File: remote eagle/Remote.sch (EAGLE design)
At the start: 30 parts, among them J1 ISP Touch, Y1 16MHz, Y2 ANTENNA2SMD5

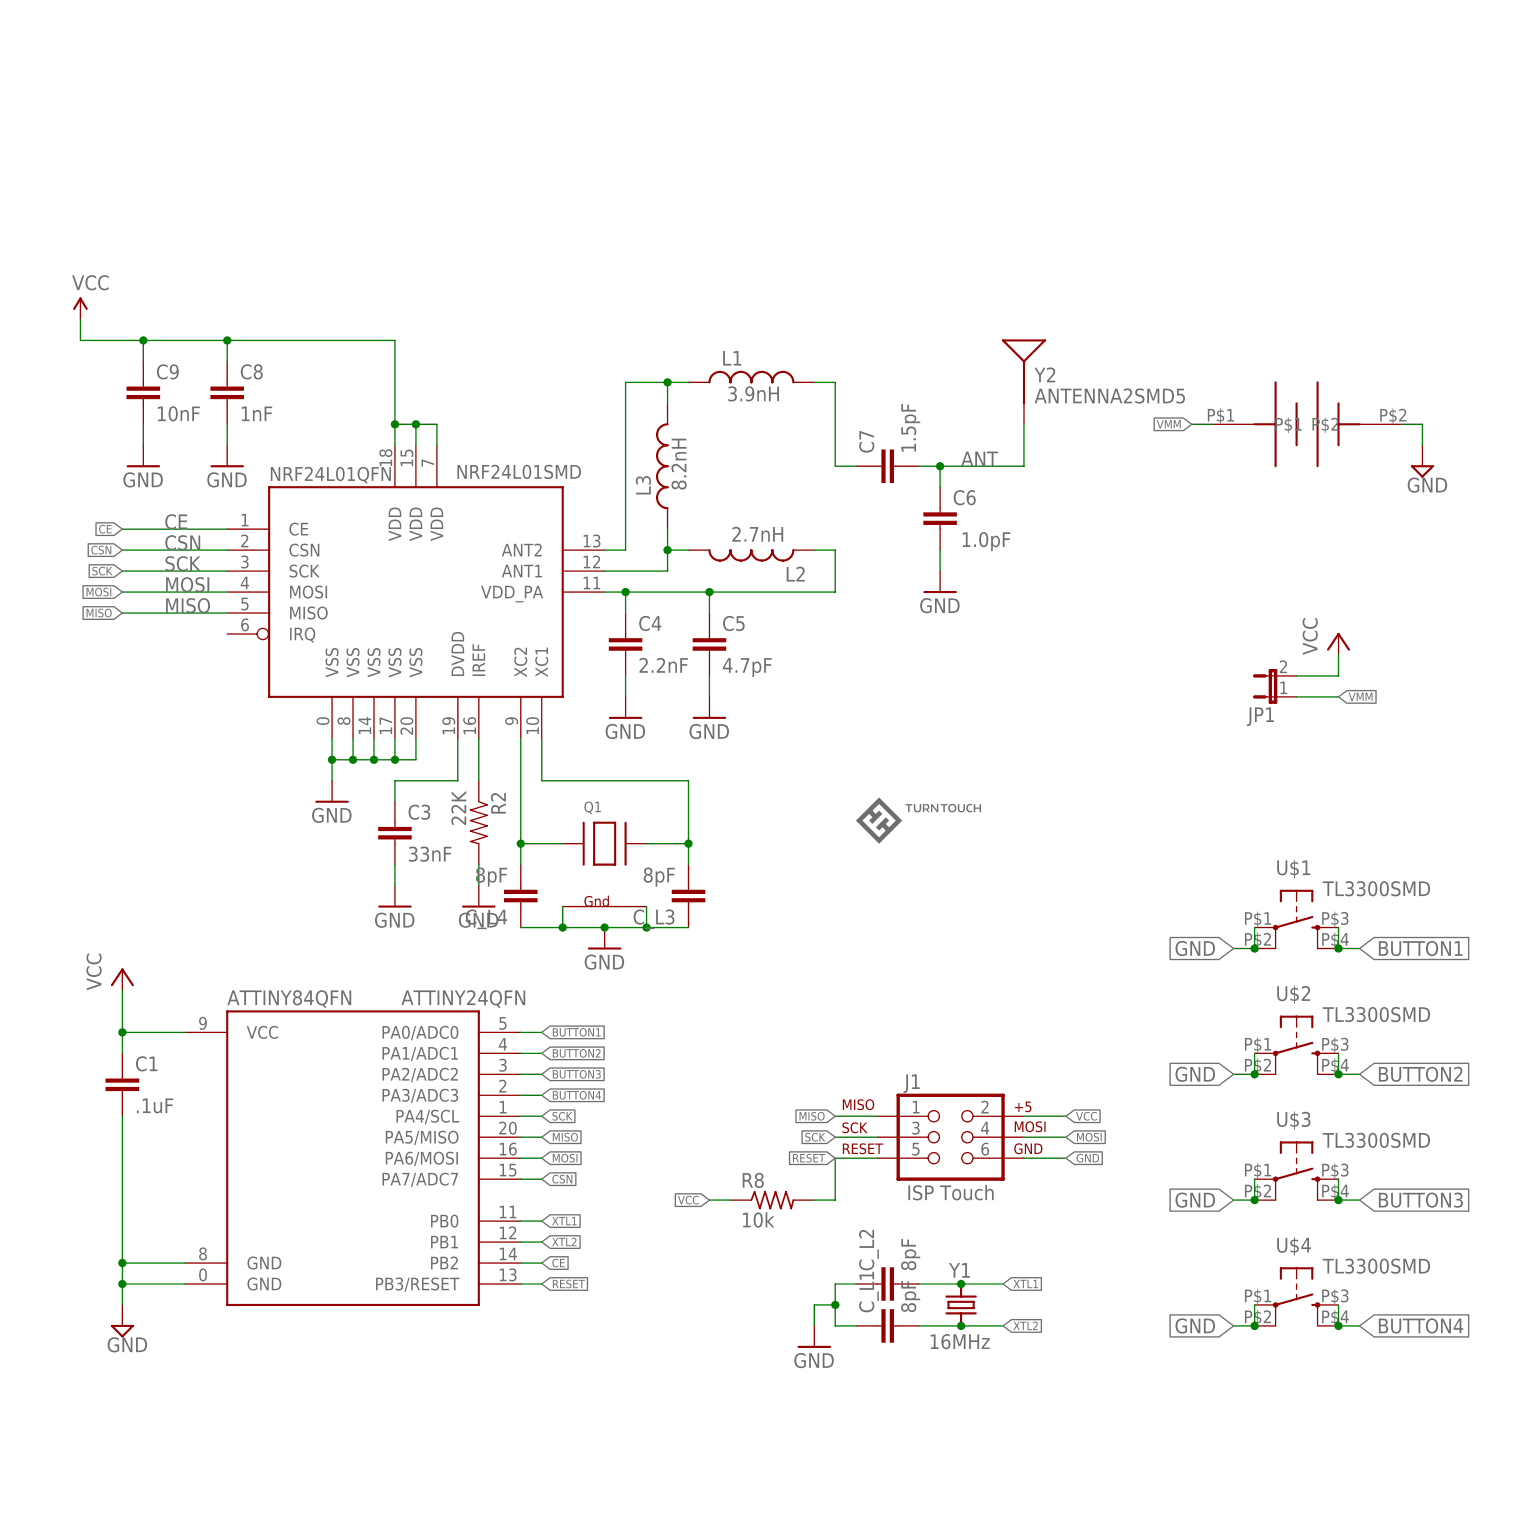
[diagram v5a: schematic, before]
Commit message: Revision 9 of the board. Could perhaps use some tweaking. Now uses atmega328p qfn chip.
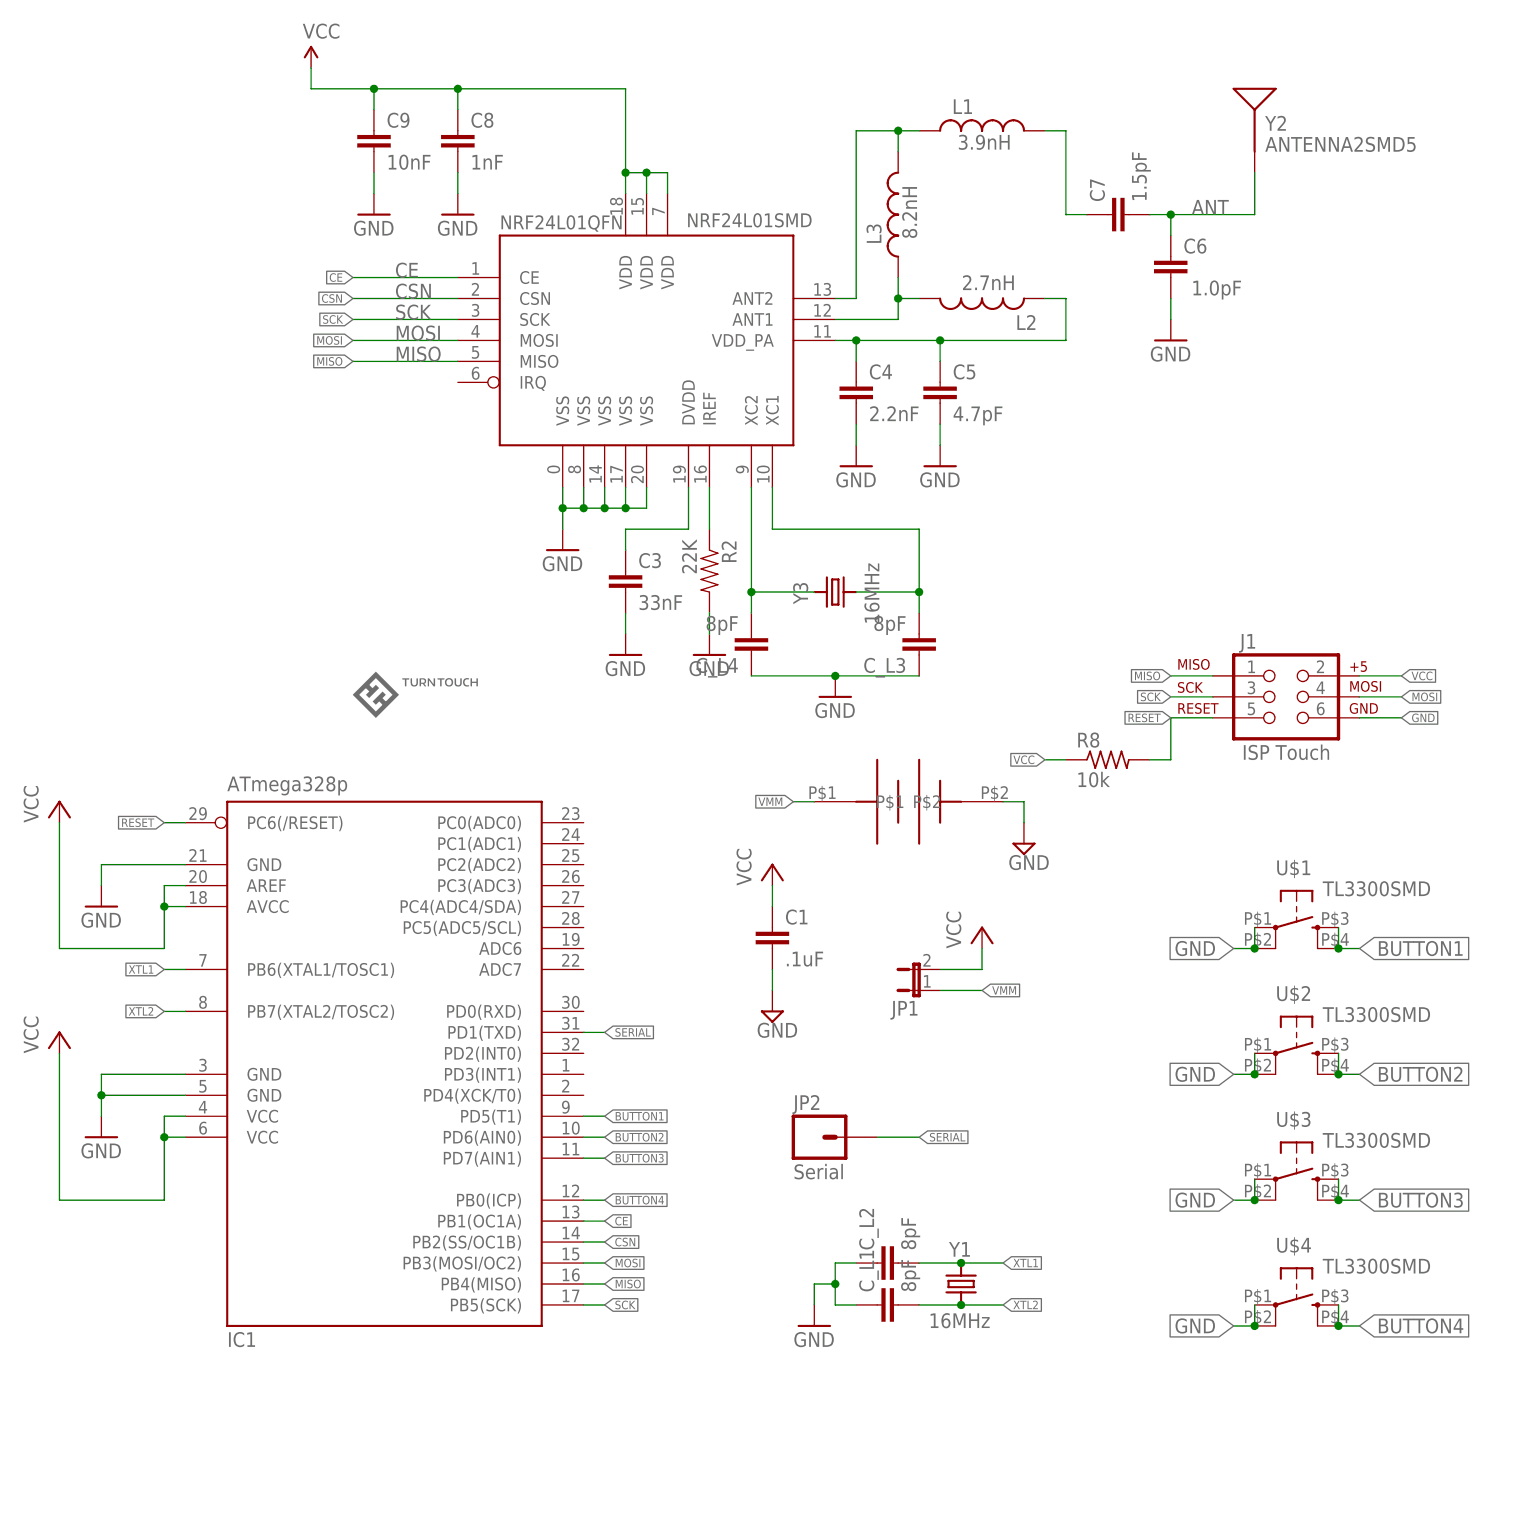
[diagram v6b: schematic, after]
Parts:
- removed ATTINY84QFN: ATTINY24QFN, SparkFun-DigitalIC:ATTINY24QFN
- removed Q1: (no value), adafruit:XTAL-4-3225
- added IC1: ATmega328p, atmel:MEGA8-MI
- added JP2: Serial, SparkFun-Connectors:M01PTH
- added Y3: 16MHz, remote:CRYSTAL5X3.2
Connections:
- new net SERIAL: IC1.PD1(TXD), JP2.1
- net BUTTON1: now also IC1.PD5(T1); no longer ATTINY84QFN.PA0/ADC0
- net BUTTON2: now also IC1.PD6(AIN0); no longer ATTINY84QFN.PA1/ADC1
- net BUTTON3: now also IC1.PD7(AIN1); no longer ATTINY84QFN.PA2/ADC2
- net BUTTON4: now also IC1.PB0(ICP); no longer ATTINY84QFN.PA3/ADC3
- net CE: now also IC1.PB1(OC1A); no longer ATTINY84QFN.PB2
- net CSN: now also IC1.PB2(SS/OC1B); no longer ATTINY84QFN.PA7/ADC7
- net GND: now also IC1.GND, IC1.GND@1, IC1.GND@2; no longer ATTINY84QFN.GND, ATTINY84QFN.GND@0, Q1.G1, Q1.G2
- net MISO: now also IC1.PB4(MISO); no longer ATTINY84QFN.PA5/MISO
- net MOSI: now also IC1.PB3(MOSI/OC2); no longer ATTINY84QFN.PA6/MOSI
- net N$2: now also Y3.2; no longer Q1.X1
- net N$3: now also Y3.1; no longer Q1.X2
- net RESET: now also IC1.PC6(/RESET); no longer ATTINY84QFN.PB3/RESET
- net SCK: now also IC1.PB5(SCK); no longer ATTINY84QFN.PA4/SCL
- net VCC: now also IC1.AREF, IC1.AVCC, IC1.VCC@1, IC1.VCC@2; no longer ATTINY84QFN.VCC
- net XTL1: now also IC1.PB6(XTAL1/TOSC1); no longer ATTINY84QFN.PB0
- net XTL2: now also IC1.PB7(XTAL2/TOSC2); no longer ATTINY84QFN.PB1
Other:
- moved on the sheet: C1, C3, C4, C5, C6, C7, C8, C9, C_L1, C_L2, C_L3, C_L4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

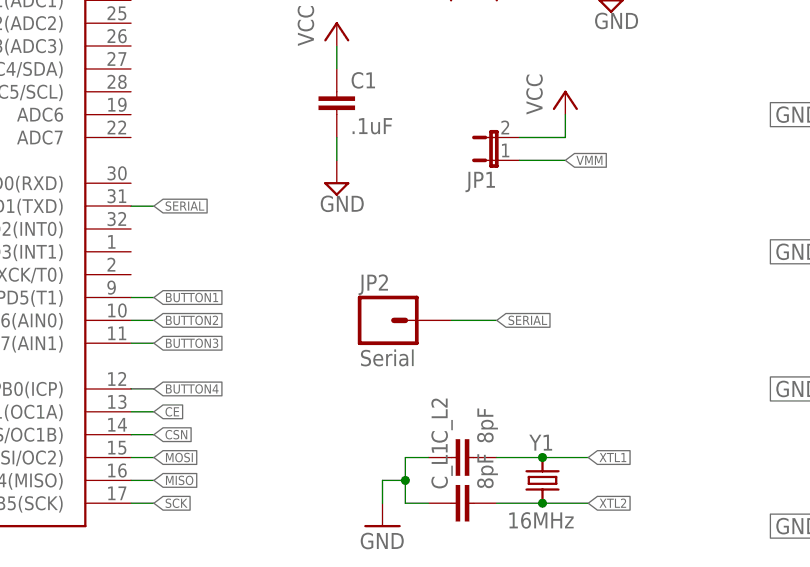
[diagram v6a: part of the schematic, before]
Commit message: Beginning rerouting for new battery holder.
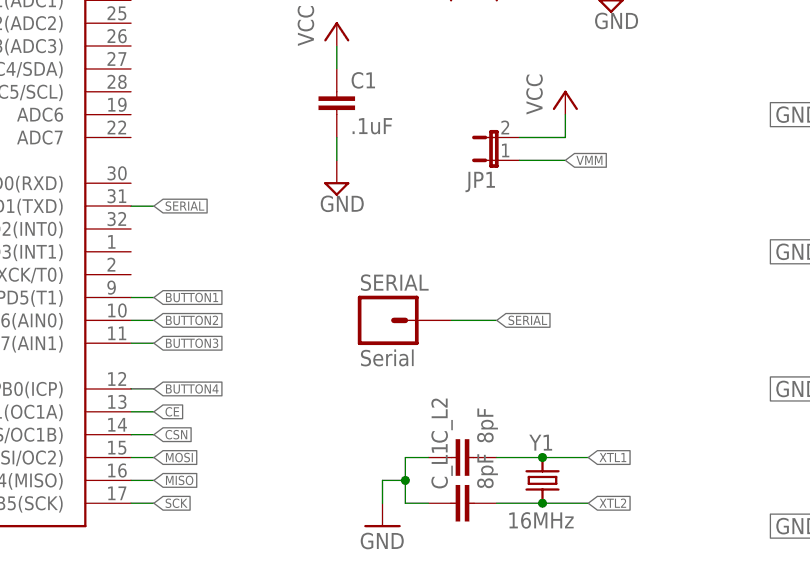
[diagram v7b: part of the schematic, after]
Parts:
- renumbered JP2 to SERIAL
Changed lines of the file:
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@@
 <part name="IC1" library="atmel" deviceset="MEGA8" device="-MI" value="ATmega328p"/>
 <part name="Y3" library="remote" deviceset="CRYSTAL" device="5X3.2" value="16MHz"/>
-<part name="JP2" library="SparkFun-Connectors" deviceset="M01" device="PTH" value="Serial"/>
+<part name="SERIAL" library="SparkFun-Connectors" deviceset="M01" device="PTH" value="Serial"/>
 <part name="GND11" library="SparkFun" deviceset="GND" device=""/>
 <part name="P+4" library="supply1" deviceset="VCC" device=""/>
@@
 <attribute name="VALUE" x="102.616" y="102.616" size="1.778" layer="96" rot="R270"/>
 </instance>
-<instance part="JP2" gate="G$1" x="96.52" y="33.02"/>
+<instance part="SERIAL" gate="G$1" x="96.52" y="33.02"/>
 <instance part="GND11" gate="1" x="10.16" y="33.02"/>
 <instance part="P+4" gate="VCC" x="5.08" y="45.72"/>
@@
 </segment>
 <segment>
-<pinref part="JP2" gate="G$1" pin="1"/>
+<pinref part="SERIAL" gate="G$1" pin="1"/>
 <wire x1="104.14" y1="33.02" x2="109.22" y2="33.02" width="0.1524" layer="91"/>
 <label x="109.22" y="33.02" size="1.016" layer="95" xref="yes"/>

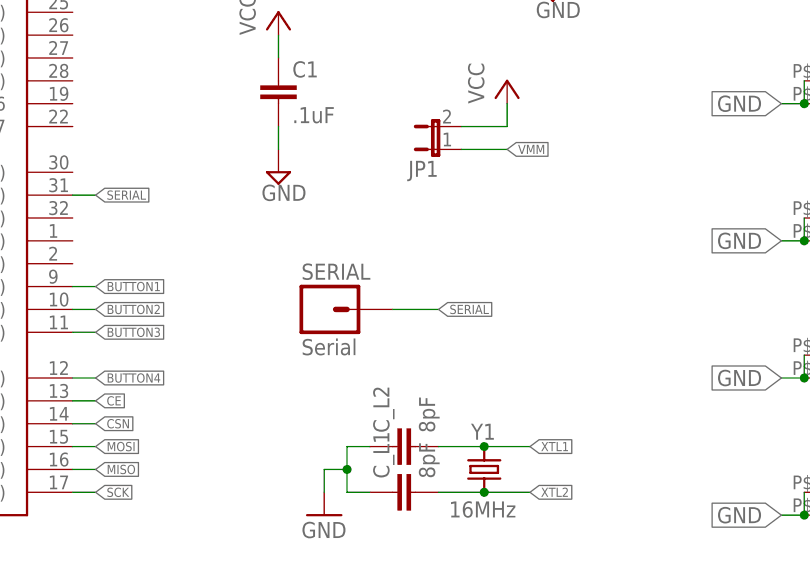
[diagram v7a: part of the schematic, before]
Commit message: Revision 10 of the board. Has fixed battery holder and improved programming header location.
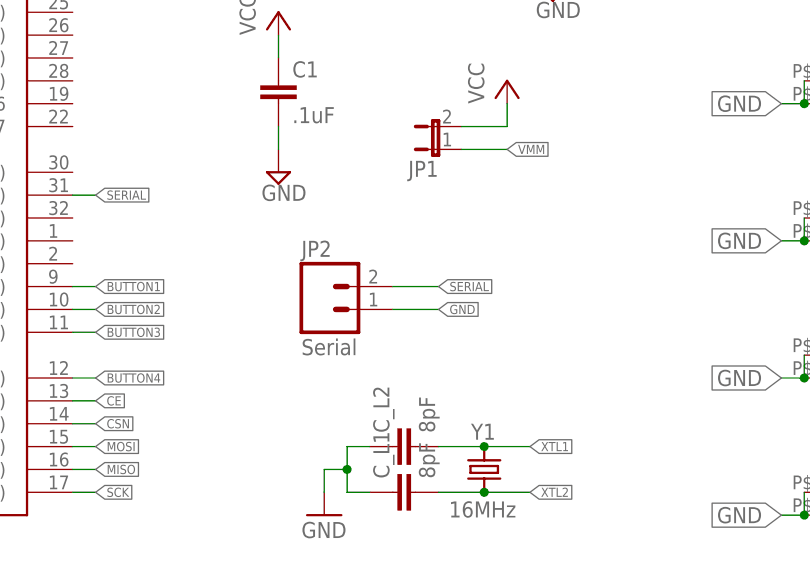
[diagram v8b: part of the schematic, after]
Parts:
- removed SERIAL: Serial, SparkFun-Connectors:M01PTH
- added JP2: Serial, SparkFun-Connectors:M02PTH
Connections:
- net GND: now also JP2.1
- net SERIAL: now also JP2.2; no longer SERIAL.1
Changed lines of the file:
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@@
 <part name="IC1" library="atmel" deviceset="MEGA8" device="-MI" value="ATmega328p"/>
 <part name="Y3" library="remote" deviceset="CRYSTAL" device="5X3.2" value="16MHz"/>
-<part name="SERIAL" library="SparkFun-Connectors" deviceset="M01" device="PTH" value="Serial"/>
 <part name="GND11" library="SparkFun" deviceset="GND" device=""/>
 <part name="P+4" library="supply1" deviceset="VCC" device=""/>
 <part name="GND12" library="SparkFun" deviceset="GND" device=""/>
 <part name="P+5" library="supply1" deviceset="VCC" device=""/>
+<part name="JP2" library="SparkFun-Connectors" deviceset="M02" device="PTH" value="Serial"/>
 </parts>
 <sheets>
@@
 <attribute name="VALUE" x="102.616" y="102.616" size="1.778" layer="96" rot="R270"/>
 </instance>
-<instance part="SERIAL" gate="G$1" x="96.52" y="33.02"/>
 <instance part="GND11" gate="1" x="10.16" y="33.02"/>
 <instance part="P+4" gate="VCC" x="5.08" y="45.72"/>
 <instance part="GND12" gate="1" x="10.16" y="60.96"/>
 <instance part="P+5" gate="VCC" x="5.08" y="73.66"/>
+<instance part="JP2" gate="G$1" x="96.52" y="33.02"/>
 </instances>
 <busses>
@@
 <wire x1="20.32" y1="66.04" x2="10.16" y2="66.04" width="0.1524" layer="91"/>
 <wire x1="10.16" y1="66.04" x2="10.16" y2="63.5" width="0.1524" layer="91"/>
+</segment>
+<segment>
+<pinref part="JP2" gate="G$1" pin="1"/>
+<wire x1="104.14" y1="33.02" x2="109.22" y2="33.02" width="0.1524" layer="91"/>
+<label x="109.22" y="33.02" size="1.016" layer="95" xref="yes"/>
 </segment>
 </net>
@@
 </segment>
 <segment>
-<pinref part="SERIAL" gate="G$1" pin="1"/>
-<wire x1="104.14" y1="33.02" x2="109.22" y2="33.02" width="0.1524" layer="91"/>
-<label x="109.22" y="33.02" size="1.016" layer="95" xref="yes"/>
+<pinref part="JP2" gate="G$1" pin="2"/>
+<wire x1="104.14" y1="35.56" x2="109.22" y2="35.56" width="0.1524" layer="91"/>
+<label x="109.22" y="35.56" size="1.016" layer="95" xref="yes"/>
 </segment>
 </net>
@@
 </sheet>
 </sheets>
-<errors>
-</errors>
 </schematic>
 </drawing>
